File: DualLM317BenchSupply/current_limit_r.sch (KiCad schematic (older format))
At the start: 13 parts, among them SW201 SP6T

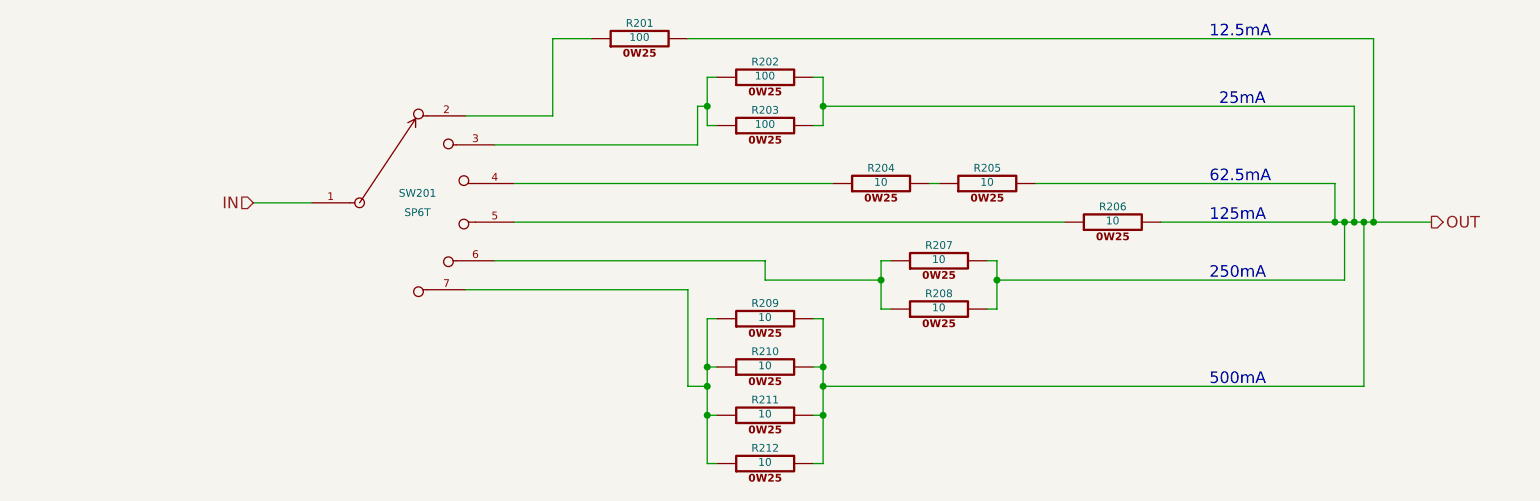
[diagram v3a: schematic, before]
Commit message: specifying 1% for current limiting resistors (lower temp co).  also, moving 10R resistors to 1/2 watt.
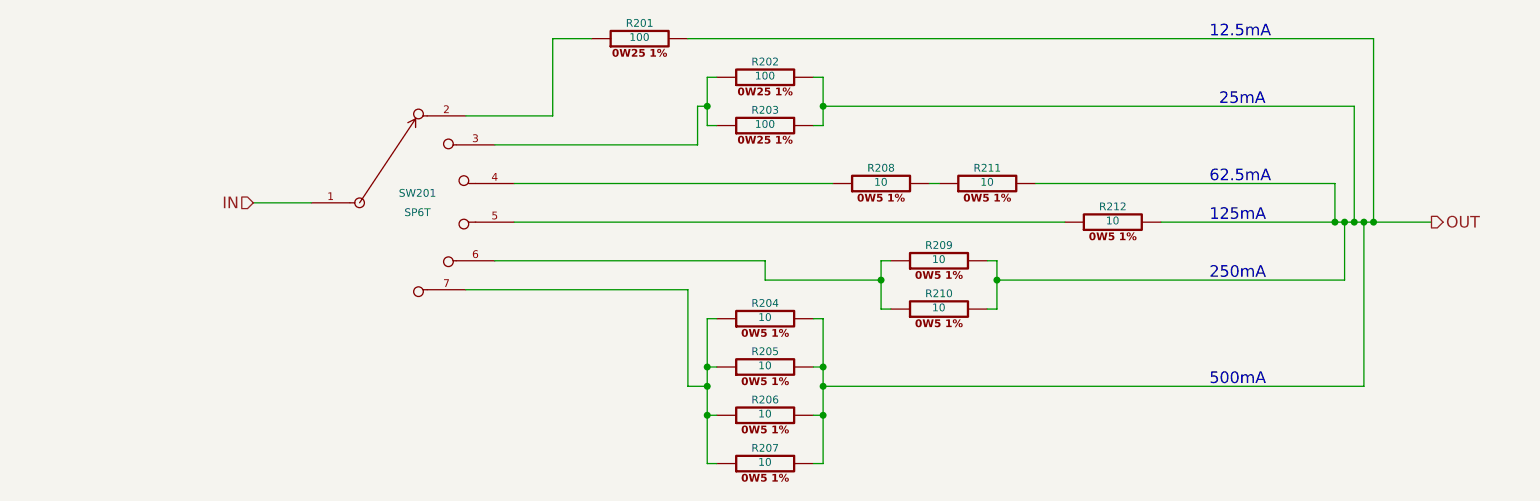
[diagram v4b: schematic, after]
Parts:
- removed R201, R202, R203: 100, ~, symbol R_0W25
- removed R204, R205, R206, R207, R208, R209, R210, R211, R212: 10, ~, symbol R_0W25
- added R201, R202, R203: 100, ~, symbol R_0W25_1PCT
- added R204, R205, R206, R207, R208, R209, R210, R211, R212: 10, ~, symbol R_0W5_1PCT
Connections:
- net OUT: now also R201.2, R202.2, R203.2, R204.2, R205.2, R206.2, R207.2, R209.2, R210.2, R211.2, R212.2
- net at SW201.5: now also R212.1
- net at SW201.4: now also R208.1
- net at SW201.6: now also R209.1, R210.1
- net at SW201.7: now also R204.1, R205.1, R206.1, R207.1
- net at SW201.2: now also R201.1
- net at SW201.3: now also R202.1, R203.1
- new net: R208.2, R211.1
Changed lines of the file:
@@
 Sheet 2 2
 Title ""
-Date "21 mar 2014"
+Date "22 mar 2014"
 Rev ""
 Comp ""
@@
 Comment4 ""
 $EndDescr
-$Comp
-L R_0W25 R206
-U 1 1 53253757
-P 7000 3900
-F 0 "R206" V 7080 3900 40  0000 C CNN
-F 1 "10" V 7007 3901 40  0000 C CNN
-F 2 "~" V 6930 3900 30  0000 C CNN
-F 3 "~" H 7000 3900 30  0000 C CNN
-	1    7000 3900
-	0    -1   -1   0
-$EndComp
-$Comp
-L R_0W25 R204
-U 1 1 5325375D
-P 5800 3700
-F 0 "R204" V 5880 3700 40  0000 C CNN
-F 1 "10" V 5807 3701 40  0000 C CNN
-F 2 "~" V 5730 3700 30  0000 C CNN
-F 3 "~" H 5800 3700 30  0000 C CNN
-	1    5800 3700
-	0    -1   -1   0
-$EndComp
-$Comp
-L R_0W25 R205
-U 1 1 53253763
-P 6350 3700
-F 0 "R205" V 6430 3700 40  0000 C CNN
-F 1 "10" V 6357 3701 40  0000 C CNN
-F 2 "~" V 6280 3700 30  0000 C CNN
-F 3 "~" H 6350 3700 30  0000 C CNN
-	1    6350 3700
-	0    -1   -1   0
-$EndComp
-$Comp
-L R_0W25 R207
-U 1 1 53253769
-P 6100 4100
-F 0 "R207" V 6180 4100 40  0000 C CNN
-F 1 "10" V 6107 4101 40  0000 C CNN
-F 2 "~" V 6030 4100 30  0000 C CNN
-F 3 "~" H 6100 4100 30  0000 C CNN
-	1    6100 4100
-	0    -1   -1   0
-$EndComp
-$Comp
-L R_0W25 R208
-U 1 1 5325376F
-P 6100 4350
-F 0 "R208" V 6180 4350 40  0000 C CNN
-F 1 "10" V 6107 4351 40  0000 C CNN
-F 2 "~" V 6030 4350 30  0000 C CNN
-F 3 "~" H 6100 4350 30  0000 C CNN
-	1    6100 4350
-	0    -1   -1   0
-$EndComp
-$Comp
-L R_0W25 R209
-U 1 1 53253775
-P 5200 4400
-F 0 "R209" V 5280 4400 40  0000 C CNN
-F 1 "10" V 5207 4401 40  0000 C CNN
-F 2 "~" V 5130 4400 30  0000 C CNN
-F 3 "~" H 5200 4400 30  0000 C CNN
-	1    5200 4400
-	0    -1   -1   0
-$EndComp
-$Comp
-L R_0W25 R210
-U 1 1 5325377B
-P 5200 4650
-F 0 "R210" V 5280 4650 40  0000 C CNN
-F 1 "10" V 5207 4651 40  0000 C CNN
-F 2 "~" V 5130 4650 30  0000 C CNN
-F 3 "~" H 5200 4650 30  0000 C CNN
-	1    5200 4650
-	0    -1   -1   0
-$EndComp
-$Comp
-L R_0W25 R211
-U 1 1 53253781
-P 5200 4900
-F 0 "R211" V 5280 4900 40  0000 C CNN
-F 1 "10" V 5207 4901 40  0000 C CNN
-F 2 "~" V 5130 4900 30  0000 C CNN
-F 3 "~" H 5200 4900 30  0000 C CNN
-	1    5200 4900
-	0    -1   -1   0
-$EndComp
-$Comp
-L R_0W25 R212
-U 1 1 53253787
-P 5200 5150
-F 0 "R212" V 5280 5150 40  0000 C CNN
-F 1 "10" V 5207 5151 40  0000 C CNN
-F 2 "~" V 5130 5150 30  0000 C CNN
-F 3 "~" H 5200 5150 30  0000 C CNN
-	1    5200 5150
-	0    -1   -1   0
-$EndComp
 Wire Wire Line
 	4950 4400 4900 4400
@@
 Wire Wire Line
 	6100 3700 6050 3700
-$Comp
-L R_0W25 R203
-U 1 1 532537AA
-P 5200 3400
-F 0 "R203" V 5280 3400 40  0000 C CNN
-F 1 "100" V 5207 3401 40  0000 C CNN
-F 2 "~" V 5130 3400 30  0000 C CNN
-F 3 "~" H 5200 3400 30  0000 C CNN
-	1    5200 3400
-	0    -1   -1   0
-$EndComp
-$Comp
-L R_0W25 R202
-U 1 1 532537B0
-P 5200 3150
-F 0 "R202" V 5280 3150 40  0000 C CNN
-F 1 "100" V 5207 3151 40  0000 C CNN
-F 2 "~" V 5130 3150 30  0000 C CNN
-F 3 "~" H 5200 3150 30  0000 C CNN
-	1    5200 3150
-	0    -1   -1   0
-$EndComp
-$Comp
-L R_0W25 R201
-U 1 1 532537B6
-P 4550 2950
-F 0 "R201" V 4630 2950 40  0000 C CNN
-F 1 "100" V 4557 2951 40  0000 C CNN
-F 2 "~" V 4480 2950 30  0000 C CNN
-F 3 "~" H 4550 2950 30  0000 C CNN
-	1    4550 2950
-	0    -1   -1   0
-$EndComp
 Wire Wire Line
 	4300 2950 4100 2950
@@
 Text HLabel 8650 3900 2    60   Output ~ 0
 OUT
+$Comp
+L R_0W25_1PCT R201
+U 1 1 532CD909
+P 4550 2950
+F 0 "R201" V 4630 2950 40  0000 C CNN
+F 1 "100" V 4557 2951 40  0000 C CNN
+F 2 "~" V 4480 2950 30  0000 C CNN
+F 3 "~" H 4550 2950 30  0000 C CNN
+	1    4550 2950
+	0    -1   -1   0
+$EndComp
+$Comp
+L R_0W25_1PCT R202
+U 1 1 532CD925
+P 5200 3150
+F 0 "R202" V 5280 3150 40  0000 C CNN
+F 1 "100" V 5207 3151 40  0000 C CNN
+F 2 "~" V 5130 3150 30  0000 C CNN
+F 3 "~" H 5200 3150 30  0000 C CNN
+	1    5200 3150
+	0    -1   -1   0
+$EndComp
+$Comp
+L R_0W25_1PCT R203
+U 1 1 532CD92B
+P 5200 3400
+F 0 "R203" V 5280 3400 40  0000 C CNN
+F 1 "100" V 5207 3401 40  0000 C CNN
+F 2 "~" V 5130 3400 30  0000 C CNN
+F 3 "~" H 5200 3400 30  0000 C CNN
+	1    5200 3400
+	0    -1   -1   0
+$EndComp
+$Comp
+L R_0W5_1PCT R208
+U 1 1 532CD933
+P 5800 3700
+F 0 "R208" V 5880 3700 40  0000 C CNN
+F 1 "10" V 5807 3701 40  0000 C CNN
+F 2 "~" V 5730 3700 30  0000 C CNN
+F 3 "~" H 5800 3700 30  0000 C CNN
+	1    5800 3700
+	0    -1   -1   0
+$EndComp
+$Comp
+L R_0W5_1PCT R211
+U 1 1 532CD94F
+P 6350 3700
+F 0 "R211" V 6430 3700 40  0000 C CNN
+F 1 "10" V 6357 3701 40  0000 C CNN
+F 2 "~" V 6280 3700 30  0000 C CNN
+F 3 "~" H 6350 3700 30  0000 C CNN
+	1    6350 3700
+	0    -1   -1   0
+$EndComp
+$Comp
+L R_0W5_1PCT R212
+U 1 1 532CD955
+P 7000 3900
+F 0 "R212" V 7080 3900 40  0000 C CNN
+F 1 "10" V 7007 3901 40  0000 C CNN
+F 2 "~" V 6930 3900 30  0000 C CNN
+F 3 "~" H 7000 3900 30  0000 C CNN
+	1    7000 3900
+	0    -1   -1   0
+$EndComp
+$Comp
+L R_0W5_1PCT R209
+U 1 1 532CD95B
+P 6100 4100
+F 0 "R209" V 6180 4100 40  0000 C CNN
+F 1 "10" V 6107 4101 40  0000 C CNN
+F 2 "~" V 6030 4100 30  0000 C CNN
+F 3 "~" H 6100 4100 30  0000 C CNN
+	1    6100 4100
+	0    -1   -1   0
+$EndComp
+$Comp
+L R_0W5_1PCT R210
+U 1 1 532CD961
+P 6100 4350
+F 0 "R210" V 6180 4350 40  0000 C CNN
+F 1 "10" V 6107 4351 40  0000 C CNN
+F 2 "~" V 6030 4350 30  0000 C CNN
+F 3 "~" H 6100 4350 30  0000 C CNN
+	1    6100 4350
+	0    -1   -1   0
+$EndComp
+$Comp
+L R_0W5_1PCT R204
+U 1 1 532CD967
+P 5200 4400
+F 0 "R204" V 5280 4400 40  0000 C CNN
+F 1 "10" V 5207 4401 40  0000 C CNN
+F 2 "~" V 5130 4400 30  0000 C CNN
+F 3 "~" H 5200 4400 30  0000 C CNN
+	1    5200 4400
+	0    -1   -1   0
+$EndComp
+$Comp
+L R_0W5_1PCT R205
+U 1 1 532CD96D
+P 5200 4650
+F 0 "R205" V 5280 4650 40  0000 C CNN
+F 1 "10" V 5207 4651 40  0000 C CNN
+F 2 "~" V 5130 4650 30  0000 C CNN
+F 3 "~" H 5200 4650 30  0000 C CNN
+	1    5200 4650
+	0    -1   -1   0
+$EndComp
+$Comp
+L R_0W5_1PCT R206
+U 1 1 532CD973
+P 5200 4900
+F 0 "R206" V 5280 4900 40  0000 C CNN
+F 1 "10" V 5207 4901 40  0000 C CNN
+F 2 "~" V 5130 4900 30  0000 C CNN
+F 3 "~" H 5200 4900 30  0000 C CNN
+	1    5200 4900
+	0    -1   -1   0
+$EndComp
+$Comp
+L R_0W5_1PCT R207
+U 1 1 532CD979
+P 5200 5150
+F 0 "R207" V 5280 5150 40  0000 C CNN
+F 1 "10" V 5207 5151 40  0000 C CNN
+F 2 "~" V 5130 5150 30  0000 C CNN
+F 3 "~" H 5200 5150 30  0000 C CNN
+	1    5200 5150
+	0    -1   -1   0
+$EndComp
 $EndSCHEMATC

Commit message: working on layout
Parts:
- removed SW201: SP6T, ~, symbol SP6T
- added SW201: DP6T, ~, symbol DP6T
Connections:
- net at R201.1: now also SW201.2
- net at R202.1, R203.1: now also SW201.3
- net at R208.1: now also SW201.4
- net at R212.1: now also SW201.5
- net at R209.1, R210.1: now also SW201.13, SW201.6
- net at R204.1, R205.1, R206.1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: now also SW201.14, SW201.7
- net OUT renamed R_LIM-
- new net R_LIM+: SW201.1, SW201.8
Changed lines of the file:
@@
 	4950 4650 4900 4650
 Connection ~ 4900 4650
-$Comp
-L SP6T SW201
-U 1 1 53253794
-P 3100 3800
-F 0 "SW201" H 3400 3850 40  0000 C CNN
-F 1 "SP6T" H 3400 3750 40  0000 C CNN
-F 2 "~" H 3100 4800 60  0000 C CNN
-F 3 "~" H 3100 4800 60  0000 C CNN
-	1    3100 3800
-	1    0    0    -1
-$EndComp
 Wire Wire Line
 	4900 4750 4800 4750
@@
 	8350 2950 8350 3900
 Connection ~ 8350 3900
-Text HLabel 2550 3800 0    60   Input ~ 0
-IN
-Wire Wire Line
-	2550 3800 2850 3800
+Text HLabel 1800 2900 0    60   Input ~ 0
+R_LIM+
 Text Notes 7500 2950 0    60   ~ 0
 12.5mA
@@
 500mA
 Text HLabel 8650 3900 2    60   Output ~ 0
-OUT
+R_LIM-
 $Comp
 L R_0W25_1PCT R201
@@
 	0    -1   -1   0
 $EndComp
+$Comp
+L DP6T SW201
+U 1 1 532F16AF
+P 3100 3800
+F 0 "SW201" H 3400 3850 40  0000 C CNN
+F 1 "DP6T" H 3400 3750 40  0000 C CNN
+F 2 "~" H 3100 4800 60  0000 C CNN
+F 3 "~" H 3100 4800 60  0000 C CNN
+	1    3100 3800
+	1    0    0    -1
+$EndComp
+Wire Wire Line
+	3900 3700 3900 3650
+Wire Wire Line
+	3900 3900 3900 3950
+Wire Wire Line
+	3100 3300 2950 3300
+Wire Wire Line
+	2950 3300 2950 4300
+Wire Wire Line
+	2950 4300 3100 4300
+Wire Wire Line
+	3100 4300 3100 4250
+Connection ~ 3100 3300
+Wire Wire Line
+	3100 3350 3100 2900
+Wire Wire Line
+	3100 2900 1800 2900
+Wire Wire Line
+	3650 4250 3650 4400
+Wire Wire Line
+	3650 4400 2150 4400
+Wire Wire Line
+	2150 4400 2150 3350
+Wire Wire Line
+	2150 3350 2550 3350
+Wire Wire Line
+	3800 4100 3800 4500
+Wire Wire Line
+	3800 4500 2050 4500
+Wire Wire Line
+	2050 4500 2050 3500
+Wire Wire Line
+	2050 3500 2400 3500
 $EndSCHEMATC
